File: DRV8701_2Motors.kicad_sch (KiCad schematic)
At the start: 47 parts, among them J1 Conn_01x02, J2 Conn_01x02, J3 Conn_01x02, J5 Conn_01x06_Socket, SW1 SW_SPDT_321

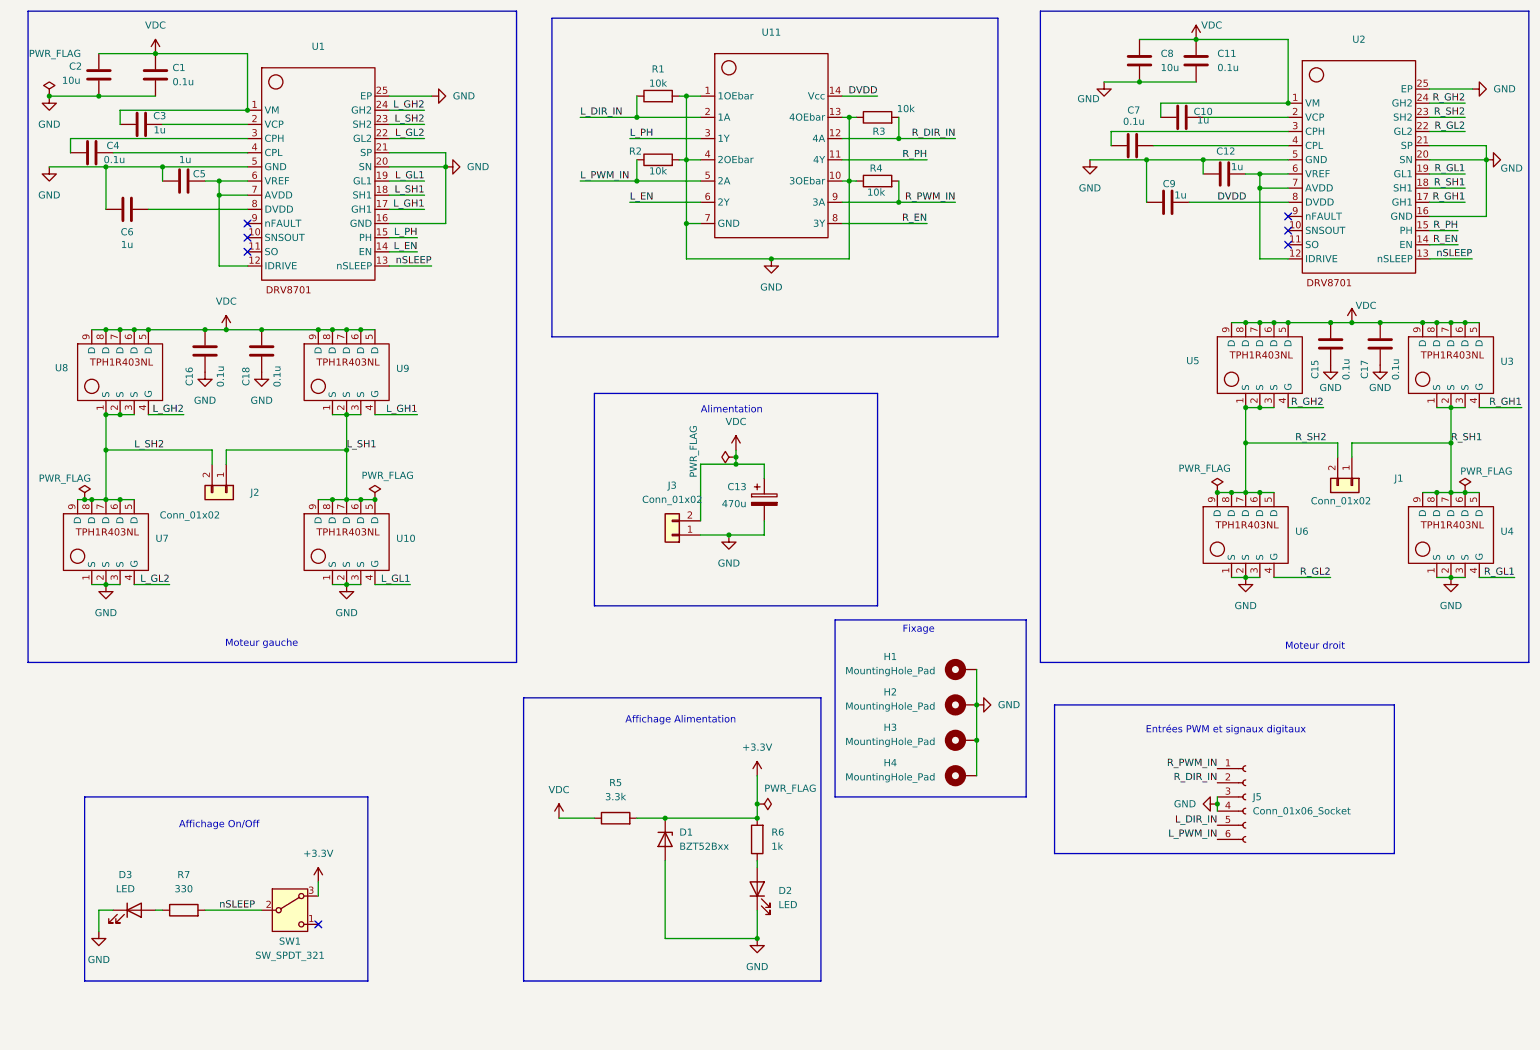
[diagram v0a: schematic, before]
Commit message: PCB V2 : adapté pour les moteurs maxons, avec l'asservissement directement dessus. Finalisation du schématique
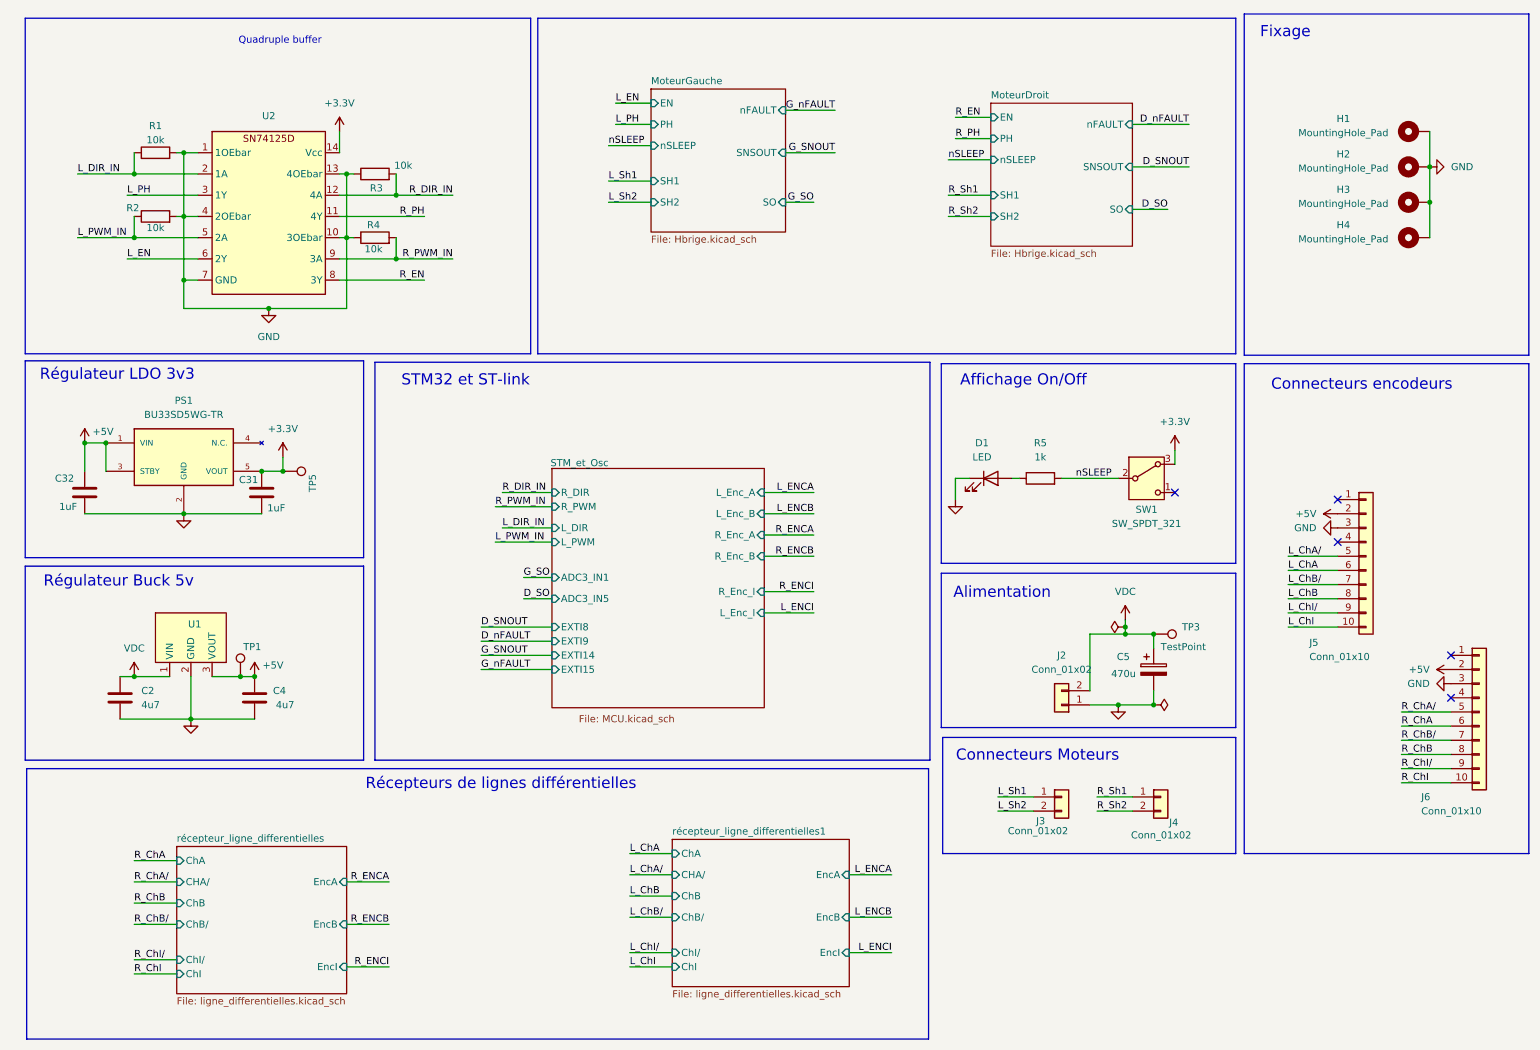
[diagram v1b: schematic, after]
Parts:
- removed C1, C11, C15, C16, C17, C18, C7: 0.1u, Capacitor_SMD:C_0402_1005Metric, symbol Device:C
- removed C10, C12, C3, C5, C6, C9: 1u, Capacitor_SMD:C_0402_1005Metric, symbol Device:C
- removed C8: 10u, Capacitor_SMD:C_0805_2012Metric, symbol Device:C
- removed D1: BZT52Bxx, Diode_SMD:D_SOD-123F, symbol Diode:BZT52Bxx
- removed D2: LED, LED_SMD:LED_0603_1608Metric_Pad1.05x0.95mm_HandSolder, symbol Device:LED
- removed J1, J2: Conn_01x02, KF301-5.0-2P:KF301-5.0-2P, symbol Connector_Generic:Conn_01x02
- removed J5: Conn_01x06_Socket, Connector_PinSocket_2.54mm:PinSocket_1x06_P2.54mm_Vertical, symbol Connector:Conn_01x06_Socket
- removed R5: 3.3k, Resistor_SMD:R_1206_3216Metric, symbol Device:R
- removed R6: 1k, Resistor_SMD:R_0603_1608Metric, symbol Device:R
- removed U1, U2: ~, DRV8701:DRV8701ERGER, symbol DRV8701:DRV8701_1
- removed U10, U3, U4, U5, U6, U7, U8, U9: ~, TPH1R403NL:TPH1R403NL, symbol DRV8701:TPH1R403NL
- added C31, C32: 1uF, Capacitor_SMD:C_0603_1608Metric_Pad1.08x0.95mm_HandSolder, symbol Device:C
- added J3, J4: Conn_01x02, KF301-5.0-2P:KF301-5.0-2P, symbol Connector_Generic:Conn_01x02
- added J5, J6: Conn_01x10, Connector_PinHeader_2.54mm:PinHeader_2x05_P2.54mm_Vertical_SMD, symbol Connector_Generic:Conn_01x10
- added PS1: BU33SD5WG-TR, BU33SD5WG-TR:SOT95P280X125-5N, symbol BU33SD5WG-TR:BU33SD5WG-TR
- added TP1, TP3, TP5: TestPoint, TestPoint:TestPoint_Pad_D1.5mm, symbol Connector:TestPoint
- added U1: ~, MagI3C:StepDown3v3, symbol MagI3C:MagI3C_3v3_StepDown
- C2: value 10u -> 4u7; footprint Capacitor_SMD:C_0805_2012Metric -> Capacitor_SMD:C_0603_1608Metric_Pad1.08x0.95mm_HandSolder
- C4: value 0.1u -> 4u7; footprint Capacitor_SMD:C_0402_1005Metric -> Capacitor_SMD:C_0603_1608Metric_Pad1.08x0.95mm_HandSolder
- R5: renamed from R7; value 330 -> 1k
- renumbered C13 to C5, D3 to D1, J3 to J2, U11 to U2
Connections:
- net DVDD is gone; now on net +3.3V: U2.14 (Vcc)
- net +3.3V: now also C31.1, PS1.5 (VOUT), TP5.1
- net GND: now also C4.2, C31.2, C32.2, J5.3 (Pin_3), J6.3 (Pin_3), PS1.2 (GND), U1.2 (GND)
- net VDC: now also TP3.1, U1.1 (VIN)
- net +5V: now reaches C4.1
- net +5V: now also C32.1, J5.2 (Pin_2), J6.2 (Pin_2), PS1.1 (VIN), PS1.3 (STBY), TP1.1, U1.3 (VOUT)
- new net L_ChA: J5.6 (Pin_6)
- new net L_ChA/: J5.5 (Pin_5)
- new net L_ChB: J5.8 (Pin_8)
- new net L_ChB/: J5.7 (Pin_7)
- new net L_ChI: J5.10 (Pin_10)
- new net L_ChI/: J5.9 (Pin_9)
- new net L_Sh1: J3.1 (Pin_1)
- new net L_Sh2: J3.2 (Pin_2)
- new net R_ChA: J6.6 (Pin_6)
- new net R_ChA/: J6.5 (Pin_5)
- new net R_ChB: J6.8 (Pin_8)
- new net R_ChB/: J6.7 (Pin_7)
- new net R_ChI: J6.10 (Pin_10)
- new net R_ChI/: J6.9 (Pin_9)
- new net R_Sh1: J4.1 (Pin_1)
- new net R_Sh2: J4.2 (Pin_2)
- no-connect marks 7 -> 5
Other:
- added sheet MoteurDroit (Hbrige.kicad_sch)
- added sheet MoteurGauche (Hbrige.kicad_sch)
- added sheet STM_et_Osc (MCU.kicad_sch)
- added sheet récepteur_ligne_differentielles (ligne_differentielles.kicad_sch)
- added sheet récepteur_ligne_differentielles1 (ligne_differentielles.kicad_sch)
- note added: "Connecteurs Moteurs"
- note added: "Connecteurs encodeurs"
- note added: "Quadruple buffer"
- note added: "Récepteurs de lignes différentielles"
- note added: "Régulateur Buck 5v"
- note added: "Régulateur LDO 3v3"
- note added: "STM32 et ST-link"
- note removed: "Affichage Alimentation"
- note removed: "Entrées PWM et signaux digitaux"
- note removed: "Moteur droit"
- note removed: "Moteur gauche"
- moved on the sheet: C5, D1, H1, H2, H3, H4, J2, R1, R2, R3, R4, R5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

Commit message: finalisation schematique
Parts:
- C5: footprint ECA1HHG471:ECA1HHG471 -> Capacitor:Wurth-470u-50V; MPN (none) -> 860080678019
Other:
- note added: "Driver & Pont en H"
- moved on the sheet: C2, C31, C32, C4, D1, J4, J5, PS1, R5, SW1, TP1, TP5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

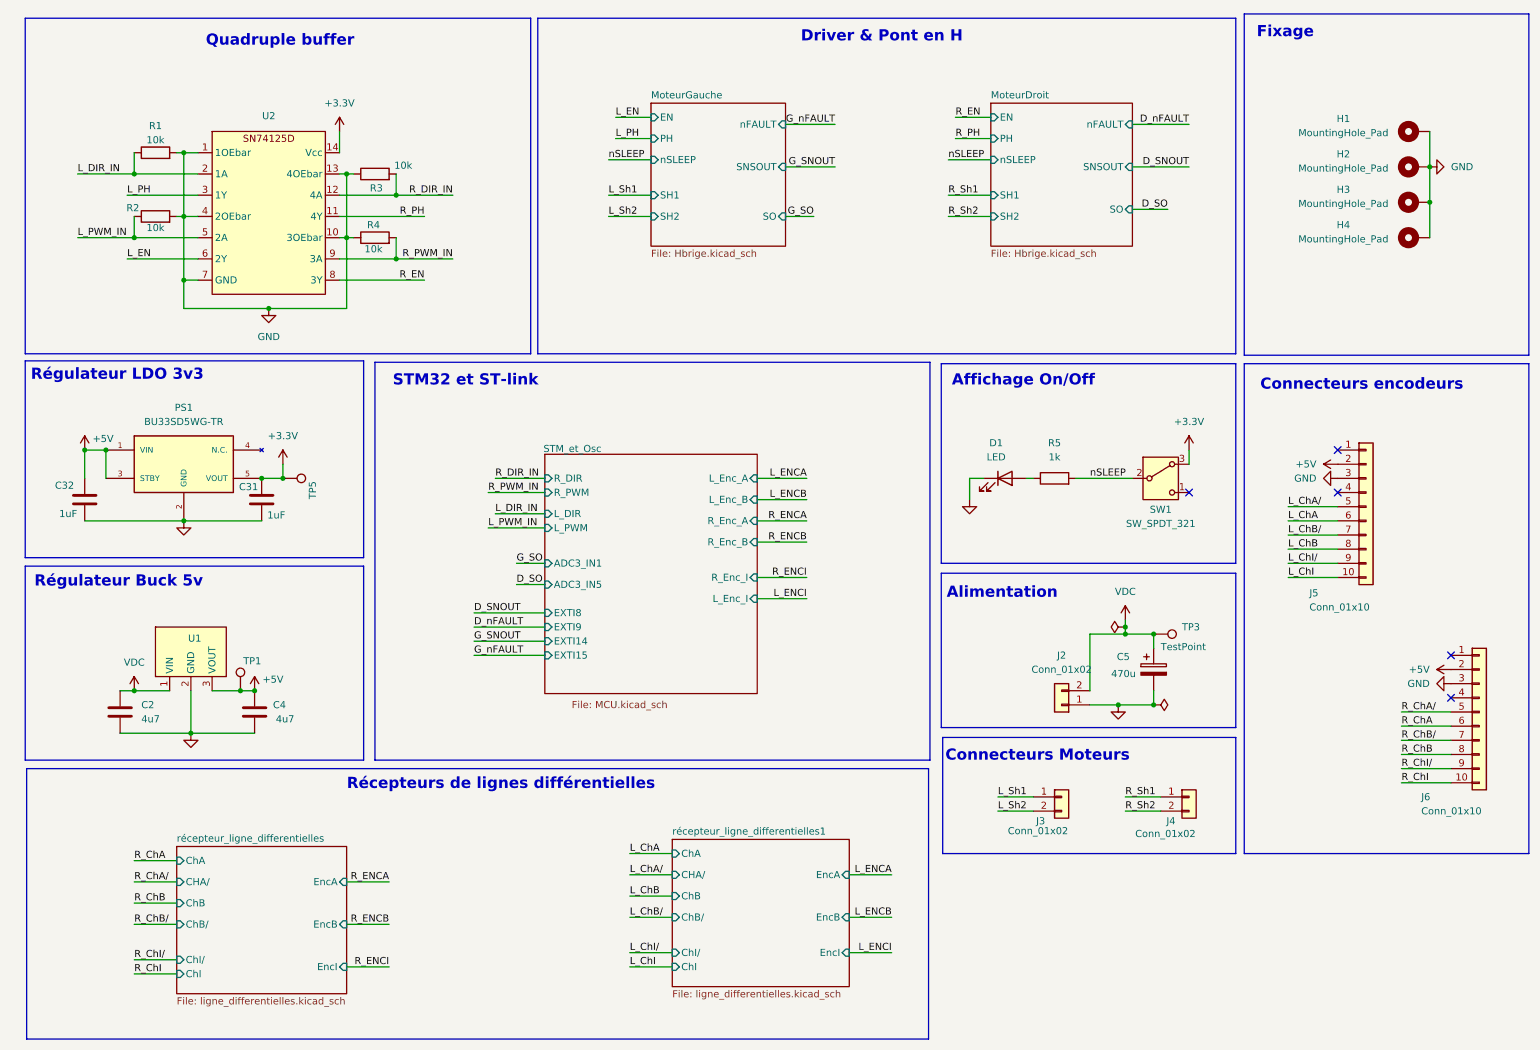
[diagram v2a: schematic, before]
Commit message: reintroduction des mosfet (au lieu des demi-ponts en H), début routage
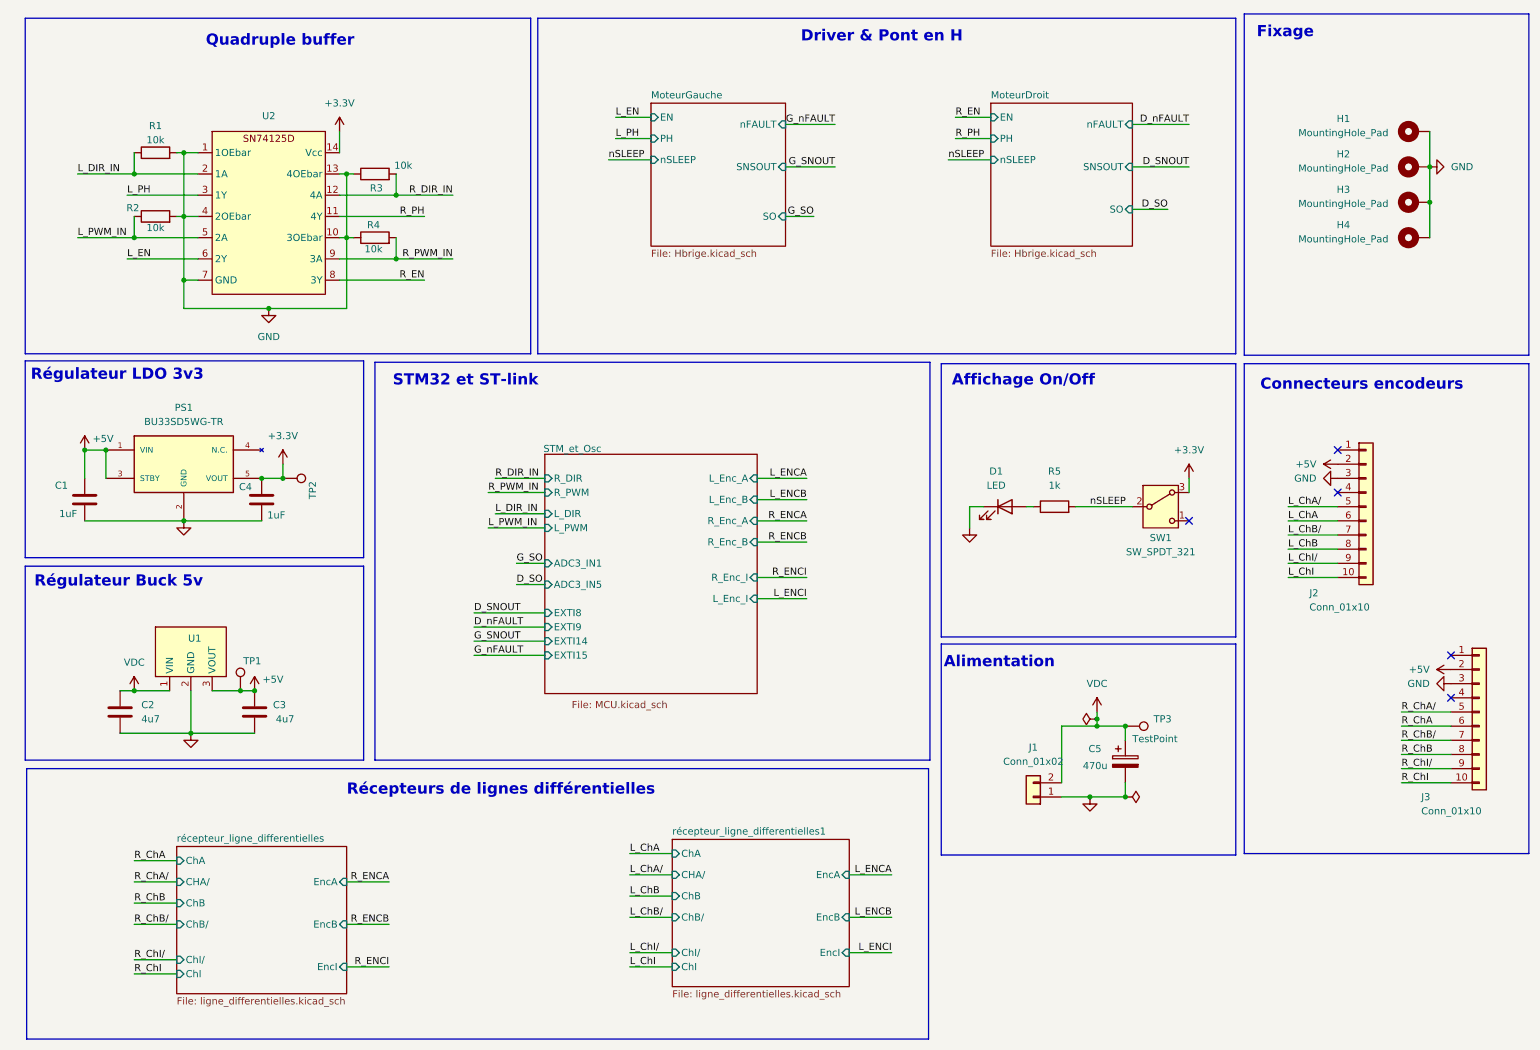
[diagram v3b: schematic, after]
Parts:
- removed J3, J4: Conn_01x02, KF301-5.0-2P:KF301-5.0-2P, symbol Connector_Generic:Conn_01x02
- C1: renamed from C32; footprint Capacitor_SMD:C_0603_1608Metric_Pad1.08x0.95mm_HandSolder -> Capacitor_SMD:C_0402_1005Metric
- C2: footprint Capacitor_SMD:C_0603_1608Metric_Pad1.08x0.95mm_HandSolder -> Capacitor_SMD:C_0402_1005Metric
- C3: renamed from C4; footprint Capacitor_SMD:C_0603_1608Metric_Pad1.08x0.95mm_HandSolder -> Capacitor_SMD:C_0402_1005Metric
- C4: renamed from C31; footprint Capacitor_SMD:C_0603_1608Metric_Pad1.08x0.95mm_HandSolder -> Capacitor_SMD:C_0402_1005Metric
- R5: footprint Resistor_SMD:R_0603_1608Metric -> Resistor_SMD:R_0402_1005Metric
- U1: MPN (none) -> 173010x78
- renumbered J2 to J1, J5 to J2, J6 to J3, TP5 to TP2
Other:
- sheet MoteurDroit ports: added none; removed SH1, SH2
- sheet MoteurGauche ports: added none; removed SH1, SH2
- note removed: "Connecteurs Moteurs"
- moved on the sheet: C5, D1, J1, R5, SW1, TP3

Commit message: maj PCB
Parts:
- removed TP3: TestPoint, TestPoint:TestPoint_Pad_D1.5mm, symbol Connector:TestPoint
- J2, J3: footprint Connector_PinHeader_2.54mm:PinHeader_2x05_P2.54mm_Vertical_SMD -> Connector_PinHeader_1.27mm:PinHeader_2x05_P1.27mm_Vertical_SMD
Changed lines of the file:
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@@
 	)
 	(junction
-		(at 210.82 140.97)
-		(diameter 0)
-		(color 0 0 0 0)
-	)
-	(junction
 		(at 210.82 153.67)
 		(diameter 0)
@@
 	)
 	(junction
-		(at 265.43 46.99)
+		(at 205.74 140.97)
 		(diameter 0)
 		(color 0 0 0 0)
 	)
 	(junction
-		(at 205.74 140.97)
+		(at 265.43 46.99)
 		(diameter 0)
 		(color 0 0 0 0)
@@
 	(wire
 		(pts
+			(xy 265.43 46.99) (xy 265.43 53.34)
+		)
+		(stroke
+			(width 0)
+			(type default)
+		)
+	)
+	(wire
+		(pts
 			(xy 153.67 104.14) (xy 144.78 104.14)
 		)
@@
 	(wire
 		(pts
-			(xy 265.43 46.99) (xy 265.43 53.34)
-		)
-		(stroke
-			(width 0)
-			(type default)
-		)
-	)
-	(wire
-		(pts
 			(xy 33.02 185.42) (xy 40.64 185.42)
 		)
@@
 	)
 	(symbol
-		(lib_id "Connector:TestPoint")
-		(at 210.82 140.97 270)
-		(unit 1)
-		(exclude_from_sim no)
-		(in_bom yes)
-		(on_board yes)
-		(dnp no)
-		(property "Reference" "TP3"
-			(at 215.9 139.6999 90)
-			(effects
-				(font
-					(size 1.27 1.27)
-				)
-				(justify left)
-			)
-		)
-		(property "Value" "TestPoint"
-			(at 212.09 143.256 90)
-			(effects
-				(font
-					(size 1.27 1.27)
-				)
-				(justify left)
-			)
-		)
-		(property "Footprint" "TestPoint:TestPoint_Pad_D1.5mm"
-			(at 210.82 146.05 0)
-			(effects
-				(font
-					(size 1.27 1.27)
-				)
-				(hide yes)
-			)
-		)
-		(property "Datasheet" "~"
-			(at 210.82 146.05 0)
-			(effects
-				(font
-					(size 1.27 1.27)
-				)
-				(hide yes)
-			)
-		)
-		(property "Description" "test point"
-			(at 210.82 140.97 0)
-			(effects
-				(font
-					(size 1.27 1.27)
-				)
-				(hide yes)
-			)
-		)
-		(pin "1"
-		)
-		(instances
-			(project "DRV8701_2Motors"
-				(path "/13741122-7bf4-473f-b117-422f29fb3018"
-					(reference "TP3")
-					(unit 1)
-				)
-			)
-		)
-	)
-	(symbol
 		(lib_id "MagI3C:MagI3C_3v3_StepDown")
 		(at 43.18 128.27 0)
@@
 			)
 		)
-		(property "Footprint" "Connector_PinHeader_2.54mm:PinHeader_2x05_P2.54mm_Vertical_SMD"
+		(property "Footprint" "Connector_PinHeader_1.27mm:PinHeader_2x05_P1.27mm_Vertical_SMD"
 			(at 254 101.6 0)
 			(effects
@@
 			)
 		)
-		(property "Footprint" "Connector_PinHeader_2.54mm:PinHeader_2x05_P2.54mm_Vertical_SMD"
+		(property "Footprint" "Connector_PinHeader_1.27mm:PinHeader_2x05_P1.27mm_Vertical_SMD"
 			(at 274.32 138.43 0)
 			(effects
